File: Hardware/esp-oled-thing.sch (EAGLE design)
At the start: 37 parts, among them Q1 2.5A/30V, U1 MCP73831, U2 TPS61200

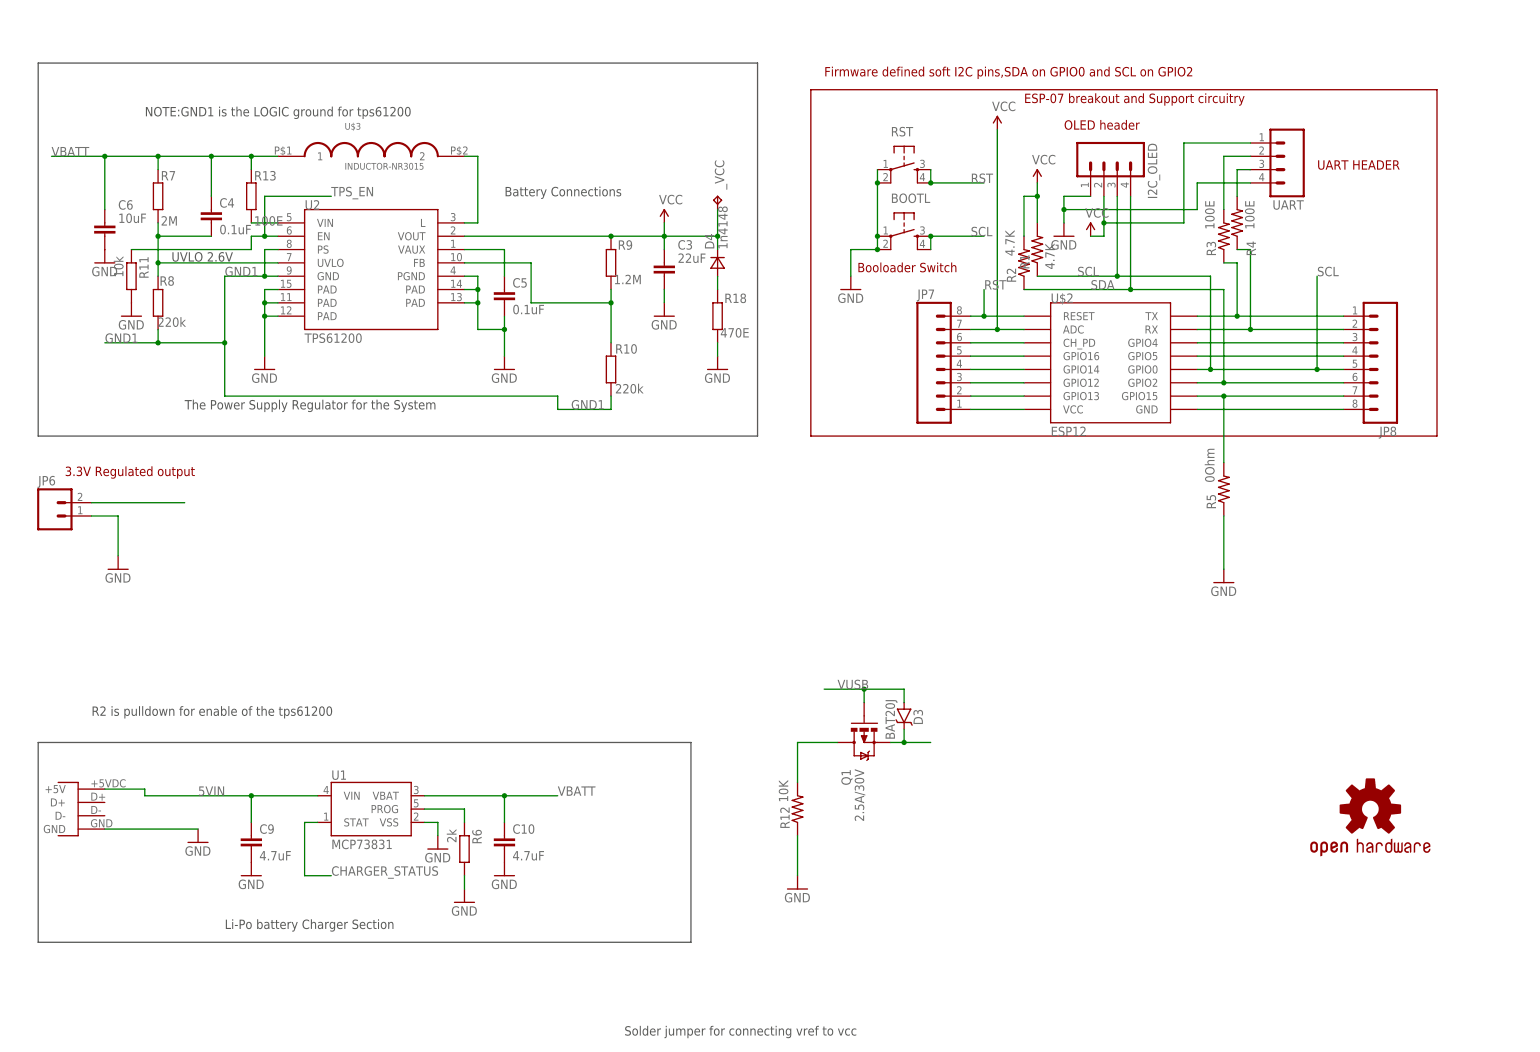
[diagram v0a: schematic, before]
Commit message: TPS61200 based system power, mc73831 lipo charger added. microusb changed to a sturdier design. some more minor bug fixes in the ESP-12 section. ability to control power (enable-disable the regulator)from the ESP module.
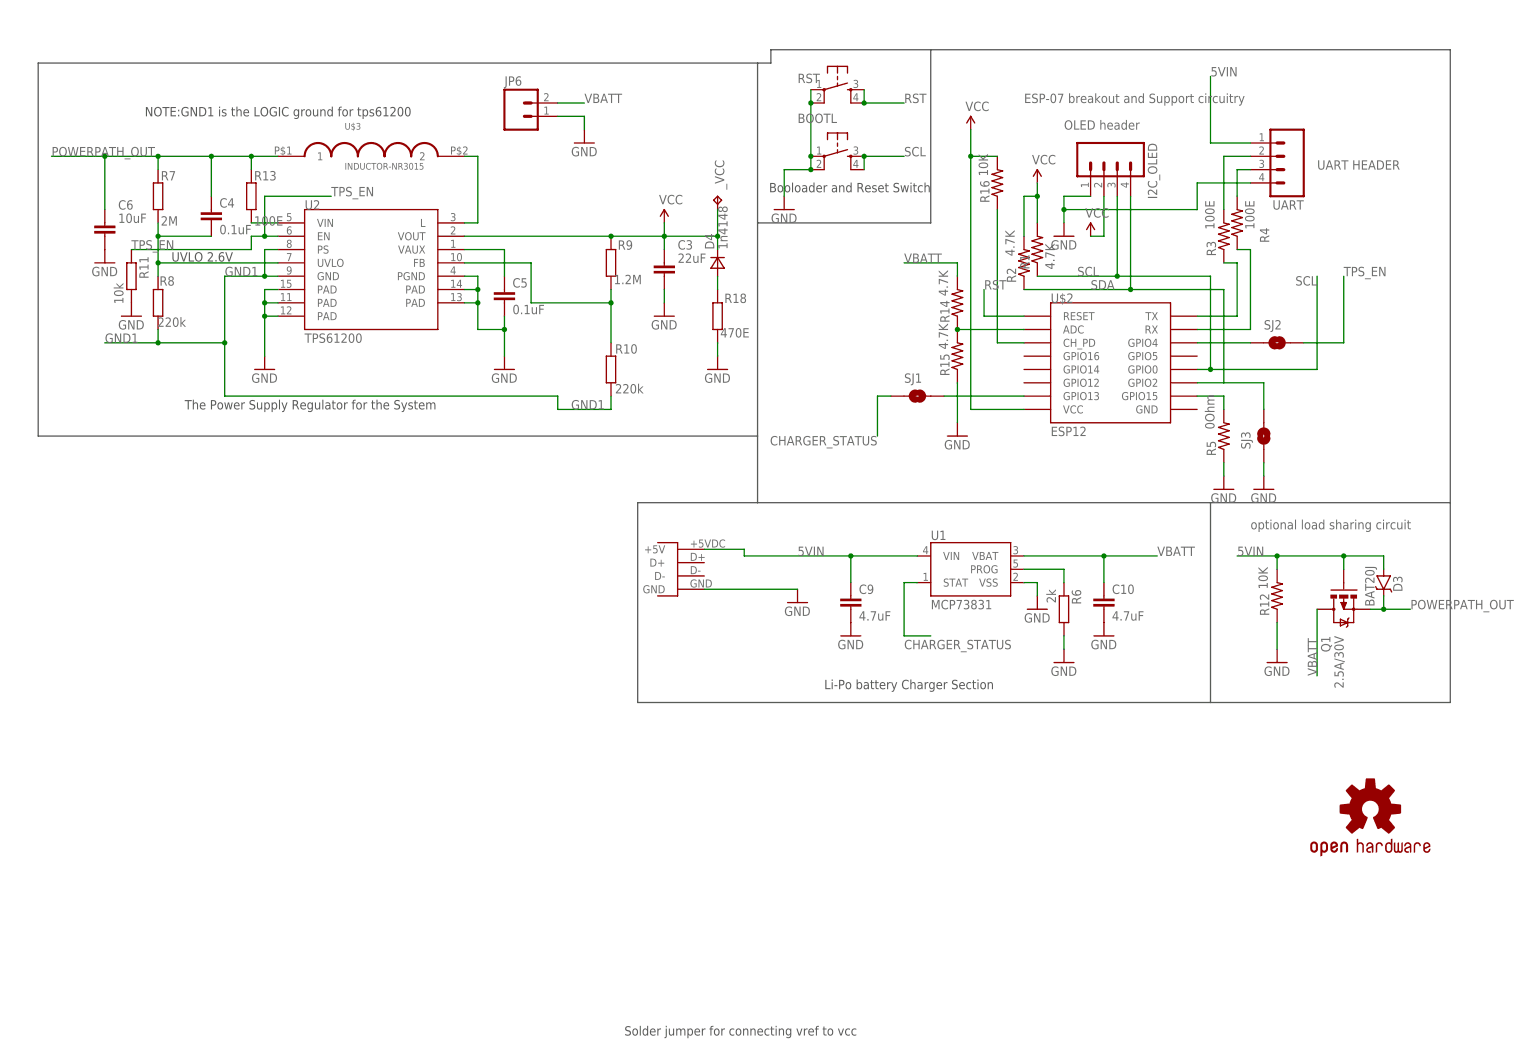
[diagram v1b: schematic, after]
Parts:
- removed JP7, JP8: (no value), SparkFun:M081X08
- added R14, R15: 4.7K, adafruit:R-US_M0805
- added R16: 10K, adafruit:R-US_M0805
- added SJ1, SJ2, SJ3: SOLDERJUMPERNO, SparkFun:SOLDERJUMPERNO
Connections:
- removed net N$11: JP8.3, U$2.GPIO4
- removed net N$12: JP8.4, U$2.GPIO5
- removed net N$16: JP8.8, U$2.GND
- removed net N$17: JP7.6, U$2.CH_PD
- removed net N$6: JP7.4, U$2.GPIO14
- removed net N$7: JP7.3, U$2.GPIO12
- removed net N$9: JP7.2, U$2.GPIO13
- removed net VBAT: JP6.2, Q1.D, R12.2
- removed net VIN1: D3.C, Q1.S
- removed net VUSB: D3.A, Q1.G
- new net N$1: SJ1.2, U$2.GPIO13
- new net N$3: R16.1, U$2.CH_PD
- new net POWERPATH_OUT: C4.1, C6.1, D3.C, Q1.S, R13.2, R7.2, U$3.1
- net 5VIN: now also D3.A, Q1.G, R12.2, UART.1
- net CHARGER_STATUS: now also SJ1.1
- net GND: now also R15.1, SJ3.1
- net N$15: no longer JP8.7
- net N$19: no longer JP8.1
- net N$2: now also R14.1, R15.2, U$2.ADC; no longer JP7.1, U$2.VCC
- net N$20: no longer JP8.2
- net N$5: now also SJ2.1, U$2.GPIO4; no longer JP7.5, U$2.GPIO16
- net RST: no longer JP7.8
- net SCL: no longer JP8.5
- net SDA: now also SJ3.2; no longer JP8.6
- net TPS_EN: now also SJ2.2
- net VBATT: now also JP6.2, Q1.D, R14.2; no longer C4.1, C6.1, R13.2, R7.2, U$3.1
- net VCC: now also R16.2, U$2.VCC; no longer JP7.7, U$2.ADC, UART.1
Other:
- note added: "Booloader and Reset Switch"
- note added: "optional load sharing circuit"
- note removed: "3.3V Regulated output"
- note removed: "Battery Connections"
- note removed: "Booloader Switch"
- note removed: "Firmware defined soft I2C pins,SDA on GPIO0 and SCL on GPIO2"
- note removed: "R2 is pulldown for enable of the tps61200"
- moved on the sheet: BOOTL, C10, C9, D3, JP6, Q1, R12, R5, R6, RST, U1

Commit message: minor shchematic changes, initial board layout started.
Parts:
- removed R5: 0Ohm, adafruit:R-US_M0805
- added SJ4: SOLDERJUMPERNO, SparkFun:SOLDERJUMPERNO
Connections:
- removed net N$15: R5.2, U$2.GPIO15
- net GND: now also SJ4.1, U$2.GPIO15; no longer R5.1
- net GND1: now also SJ4.2
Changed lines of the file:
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@@
 <part name="GND19" library="SparkFun" deviceset="GND" device=""/>
 <part name="R18" library="rcl" deviceset="R-EU_" device="R0402" value="470E"/>
-<part name="R5" library="adafruit" deviceset="R-US_" device="M0805" value="0Ohm"/>
 <part name="GND1" library="supply1" deviceset="GND" device=""/>
 <part name="P+1" library="SparkFun" deviceset="VCC" device=""/>
@@
 <part name="SJ3" library="SparkFun" deviceset="SOLDERJUMPER" device="NO"/>
 <part name="GND7" library="supply1" deviceset="GND" device=""/>
+<part name="SJ4" library="SparkFun" deviceset="SOLDERJUMPER" device="NO"/>
+<part name="GND15" library="SparkFun" deviceset="GND" device=""/>
 </parts>
 <sheets>
@@
 <attribute name="VALUE" x="132.588" y="122.936" size="1.778" layer="96"/>
 </instance>
-<instance part="R5" gate="G$1" x="228.6" y="104.14" smashed="yes" rot="R90">
-<attribute name="NAME" x="227.1014" y="100.33" size="1.778" layer="95" rot="R90"/>
-<attribute name="VALUE" x="226.822" y="105.41" size="1.778" layer="96" rot="R90"/>
-</instance>
 <instance part="GND1" gate="1" x="228.6" y="93.98"/>
 <instance part="P+1" gate="1" x="180.34" y="162.56"/>
@@
 </instance>
 <instance part="GND7" gate="1" x="236.22" y="93.98"/>
+<instance part="SJ4" gate="1" x="15.24" y="116.84" smashed="yes" rot="R90">
+<attribute name="NAME" x="12.7" y="114.3" size="1.778" layer="95" rot="R90"/>
+</instance>
+<instance part="GND15" gate="1" x="15.24" y="106.68" smashed="yes">
+<attribute name="VALUE" x="12.7" y="104.14" size="1.778" layer="96"/>
+</instance>
 </instances>
 <busses>
@@
 </segment>
 <segment>
-<pinref part="R5" gate="G$1" pin="1"/>
 <pinref part="GND1" gate="1" pin="GND"/>
-<wire x1="228.6" y1="96.52" x2="228.6" y2="99.06" width="0.1524" layer="91"/>
+<wire x1="223.52" y1="111.76" x2="228.6" y2="111.76" width="0.1524" layer="91"/>
+<pinref part="U$2" gate="G$1" pin="GPIO15"/>
+<wire x1="228.6" y1="111.76" x2="228.6" y2="96.52" width="0.1524" layer="91"/>
 </segment>
 <segment>
@@
 <pinref part="GND7" gate="1" pin="GND"/>
 <wire x1="236.22" y1="99.06" x2="236.22" y2="96.52" width="0.1524" layer="91"/>
+</segment>
+<segment>
+<pinref part="SJ4" gate="1" pin="1"/>
+<pinref part="GND15" gate="1" pin="GND"/>
+<wire x1="15.24" y1="109.22" x2="15.24" y2="111.76" width="0.1524" layer="91"/>
 </segment>
 </net>
@@
 <wire x1="228.6" y1="114.3" x2="236.22" y2="114.3" width="0.1524" layer="91"/>
 <wire x1="236.22" y1="114.3" x2="236.22" y2="109.22" width="0.1524" layer="91"/>
-</segment>
-</net>
-<net name="N$15" class="0">
-<segment>
-<wire x1="223.52" y1="111.76" x2="228.6" y2="111.76" width="0.1524" layer="91"/>
-<pinref part="U$2" gate="G$1" pin="GPIO15"/>
-<pinref part="R5" gate="G$1" pin="2"/>
-<wire x1="228.6" y1="111.76" x2="228.6" y2="109.22" width="0.1524" layer="91"/>
+<junction x="228.6" y="114.3"/>
 </segment>
 </net>
@@
 <junction x="25.4" y="121.92"/>
 <junction x="38.1" y="121.92"/>
-</segment>
-</net>
+<pinref part="SJ4" gate="1" pin="2"/>
+</segment>
+</net>

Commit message: minor layout modifications
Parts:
- added S1: TL39PO, switch:TL39PO
- added SJ5: (no value), jumper:SJ2W
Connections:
- new net SYSPOWER_IN: C4.1, C6.1, R13.2, R7.2, SJ5.2, U$3.1
- net POWERPATH_OUT: now also SJ5.3; no longer C4.1, C6.1, R13.2, R7.2, U$3.1
- net TPS_EN: now also S1.P
- net VBATT: now also SJ5.1
- net VCC: now also S1.O
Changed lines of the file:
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@@
 <?xml version="1.0" encoding="utf-8"?>
 <!DOCTYPE eagle SYSTEM "eagle.dtd">
-<eagle version="6.2">
+<eagle version="7.3.0">
 <drawing>
 <settings>
@@
 <part name="SJ4" library="SparkFun" deviceset="SOLDERJUMPER" device="NO"/>
 <part name="GND15" library="SparkFun" deviceset="GND" device=""/>
+<part name="SJ5" library="jumper" deviceset="SJ2W" device=""/>
+<part name="S1" library="switch" deviceset="TL39PO" device=""/>
+<part name="P+5" library="SparkFun" deviceset="VCC" device=""/>
 </parts>
 <sheets>
@@
 <attribute name="VALUE" x="12.7" y="104.14" size="1.778" layer="96"/>
 </instance>
+<instance part="SJ5" gate="G$1" x="5.08" y="149.86" rot="R180"/>
+<instance part="S1" gate="BEF1" x="53.34" y="86.36" rot="R270"/>
+<instance part="P+5" gate="1" x="71.12" y="91.44"/>
 </instances>
 <busses>
@@
 <junction x="180.34" y="157.48"/>
 </segment>
+<segment>
+<pinref part="S1" gate="BEF1" pin="O"/>
+<wire x1="58.42" y1="88.9" x2="71.12" y2="88.9" width="0.1524" layer="91"/>
+<pinref part="P+5" gate="1" pin="VCC"/>
+<wire x1="71.12" y1="91.44" x2="71.12" y2="88.9" width="0.1524" layer="91"/>
+</segment>
 </net>
 <net name="N$19" class="0">
@@
 <wire x1="177.8" y1="137.16" x2="167.64" y2="137.16" width="0.1524" layer="91"/>
 <label x="167.64" y="137.16" size="1.778" layer="95"/>
+</segment>
+<segment>
+<pinref part="SJ5" gate="G$1" pin="1"/>
+<wire x1="5.08" y1="144.78" x2="5.08" y2="134.62" width="0.1524" layer="91"/>
+<label x="5.08" y="134.62" size="1.778" layer="95" rot="R270"/>
 </segment>
 </net>
@@
 <label x="251.46" y="134.62" size="1.778" layer="95"/>
 </segment>
+<segment>
+<pinref part="S1" gate="BEF1" pin="P"/>
+<wire x1="48.26" y1="86.36" x2="33.02" y2="86.36" width="0.1524" layer="91"/>
+<wire x1="33.02" y1="86.36" x2="33.02" y2="88.9" width="0.1524" layer="91"/>
+<label x="33.02" y="88.9" size="1.778" layer="95"/>
+</segment>
 </net>
 <net name="CHARGER_STATUS" class="0">
@@
 </segment>
 <segment>
+<pinref part="SJ5" gate="G$1" pin="3"/>
+<wire x1="5.08" y1="154.94" x2="5.08" y2="162.56" width="0.1524" layer="91"/>
+<label x="5.08" y="162.56" size="1.778" layer="95" rot="R90"/>
+</segment>
+</net>
+<net name="N$1" class="0">
+<segment>
+<pinref part="SJ1" gate="1" pin="2"/>
+<pinref part="U$2" gate="G$1" pin="GPIO13"/>
+<wire x1="175.26" y1="111.76" x2="190.5" y2="111.76" width="0.1524" layer="91"/>
+</segment>
+</net>
+<net name="N$2" class="0">
+<segment>
+<pinref part="U$2" gate="G$1" pin="ADC"/>
+<wire x1="190.5" y1="124.46" x2="177.8" y2="124.46" width="0.1524" layer="91"/>
+<pinref part="R14" gate="G$1" pin="1"/>
+<pinref part="R15" gate="G$1" pin="2"/>
+<junction x="177.8" y="124.46"/>
+</segment>
+</net>
+<net name="N$3" class="0">
+<segment>
+<pinref part="U$2" gate="G$1" pin="CH_PD"/>
+<wire x1="190.5" y1="121.92" x2="185.42" y2="121.92" width="0.1524" layer="91"/>
+<wire x1="185.42" y1="121.92" x2="185.42" y2="147.32" width="0.1524" layer="91"/>
+<pinref part="R16" gate="G$1" pin="1"/>
+</segment>
+</net>
+<net name="N$5" class="0">
+<segment>
+<pinref part="U$2" gate="G$1" pin="GPIO4"/>
+<pinref part="SJ2" gate="1" pin="1"/>
+<wire x1="223.52" y1="121.92" x2="233.68" y2="121.92" width="0.1524" layer="91"/>
+</segment>
+</net>
+<net name="SYSPOWER_IN" class="0">
+<segment>
 <wire x1="25.4" y1="154.94" x2="25.4" y2="157.48" width="0.1524" layer="91"/>
 <wire x1="25.4" y1="157.48" x2="35.56" y2="157.48" width="0.1524" layer="91"/>
@@
 <wire x1="15.24" y1="157.48" x2="25.4" y2="157.48" width="0.1524" layer="91"/>
 <wire x1="35.56" y1="149.86" x2="35.56" y2="157.48" width="0.1524" layer="91"/>
-<wire x1="5.08" y1="157.48" x2="15.24" y2="157.48" width="0.1524" layer="91"/>
 <junction x="25.4" y="157.48"/>
 <junction x="15.24" y="157.48"/>
 <junction x="35.56" y="157.48"/>
-<label x="5.08" y="157.48" size="1.778" layer="95"/>
+<label x="15.24" y="157.48" size="1.778" layer="95"/>
 <pinref part="C4" gate="G$1" pin="1"/>
 <pinref part="R7" gate="G$1" pin="2"/>
@@
 <pinref part="U$3" gate="G$1" pin="1"/>
 <pinref part="R13" gate="G$1" pin="2"/>
+<wire x1="10.16" y1="157.48" x2="15.24" y2="157.48" width="0.1524" layer="91"/>
 <wire x1="43.18" y1="154.94" x2="43.18" y2="157.48" width="0.1524" layer="91"/>
 <junction x="43.18" y="157.48"/>
-</segment>
-</net>
-<net name="N$1" class="0">
-<segment>
-<pinref part="SJ1" gate="1" pin="2"/>
-<pinref part="U$2" gate="G$1" pin="GPIO13"/>
-<wire x1="175.26" y1="111.76" x2="190.5" y2="111.76" width="0.1524" layer="91"/>
-</segment>
-</net>
-<net name="N$2" class="0">
-<segment>
-<pinref part="U$2" gate="G$1" pin="ADC"/>
-<wire x1="190.5" y1="124.46" x2="177.8" y2="124.46" width="0.1524" layer="91"/>
-<pinref part="R14" gate="G$1" pin="1"/>
-<pinref part="R15" gate="G$1" pin="2"/>
-<junction x="177.8" y="124.46"/>
-</segment>
-</net>
-<net name="N$3" class="0">
-<segment>
-<pinref part="U$2" gate="G$1" pin="CH_PD"/>
-<wire x1="190.5" y1="121.92" x2="185.42" y2="121.92" width="0.1524" layer="91"/>
-<wire x1="185.42" y1="121.92" x2="185.42" y2="147.32" width="0.1524" layer="91"/>
-<pinref part="R16" gate="G$1" pin="1"/>
-</segment>
-</net>
-<net name="N$5" class="0">
-<segment>
-<pinref part="U$2" gate="G$1" pin="GPIO4"/>
-<pinref part="SJ2" gate="1" pin="1"/>
-<wire x1="223.52" y1="121.92" x2="233.68" y2="121.92" width="0.1524" layer="91"/>
-</segment>
-</net>
+<pinref part="SJ5" gate="G$1" pin="2"/>
+<wire x1="10.16" y1="149.86" x2="10.16" y2="157.48" width="0.1524" layer="91"/>
+</segment>
+</net>
